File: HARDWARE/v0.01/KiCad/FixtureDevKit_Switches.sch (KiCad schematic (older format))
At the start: 64 parts, among them J10 LED_3, J106 LED_6, J107 LED_7, J11 SW_5, J12 LED_4, J13 SW_6, J14 LED_5, J15 SW_7, J2 LED_0, J3 SW_0, J4 SW_1, J5 LED_1, J6 SW_2, J7 LED_2, J8 SW_3, J9 SW_4, SW1 GTS203211B, SW2 GTS203211B, SW3 GTS203211B, SW4 GTS203211B, SW5 GTS203211B, SW6 GTS203211B, SW7 GTS203211B, SW8 GTS203211B

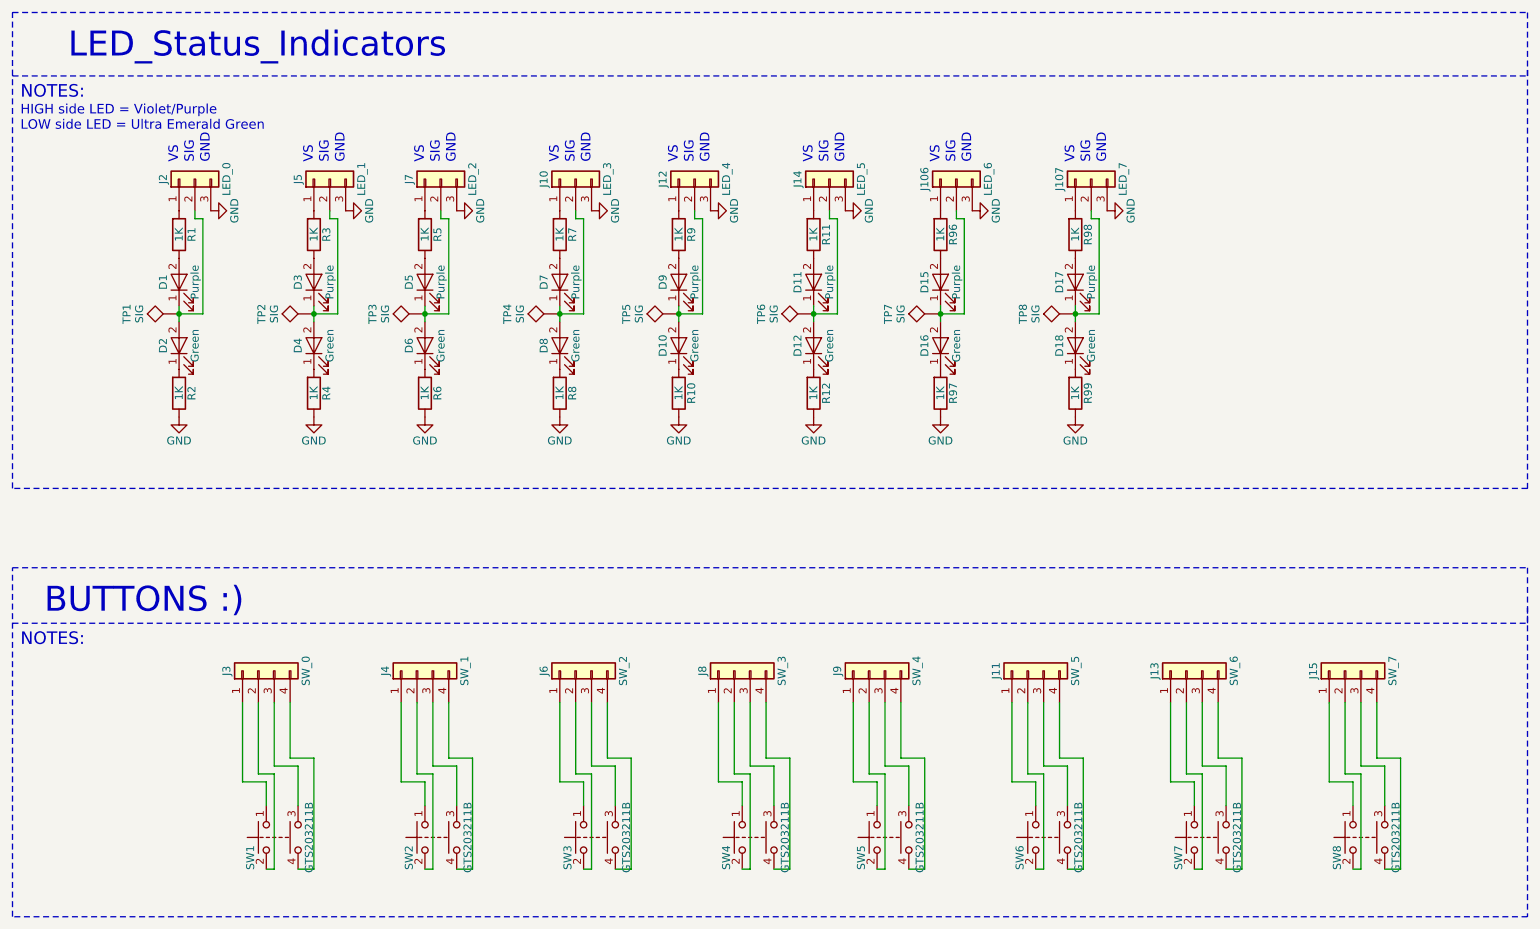
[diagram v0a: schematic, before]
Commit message: quasi-redoing entire schematic and layout
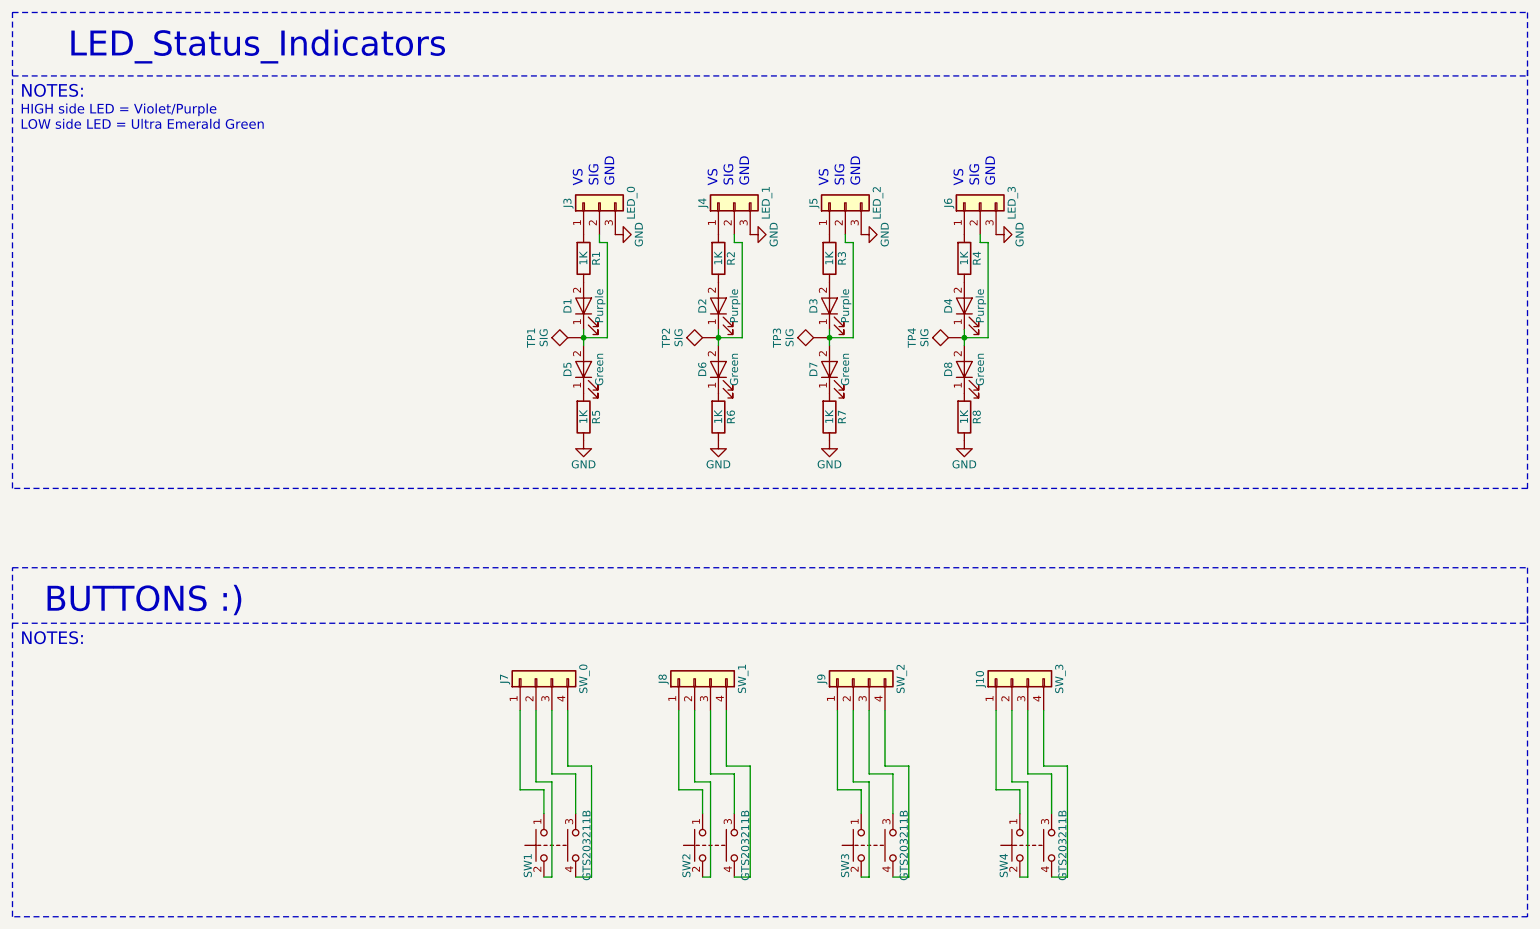
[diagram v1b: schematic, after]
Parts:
- removed D10, D12, D16, D18: Green, LEDs:LED_0805_HandSoldering, symbol LED
- removed D11, D15, D17, D9: Purple, LEDs:LED_0805_HandSoldering, symbol LED
- removed J106: LED_6, Pin_Headers:Pin_Header_Straight_1x03_Pitch2.54mm, symbol Conn_01x03
- removed J107: LED_7, Pin_Headers:Pin_Header_Straight_1x03_Pitch2.54mm, symbol Conn_01x03
- removed J11: SW_5, Pin_Headers:Pin_Header_Straight_1x04_Pitch2.54mm, symbol Conn_01x04
- removed J12: LED_4, Pin_Headers:Pin_Header_Straight_1x03_Pitch2.54mm, symbol Conn_01x03
- removed J13: SW_6, Pin_Headers:Pin_Header_Straight_1x04_Pitch2.54mm, symbol Conn_01x04
- removed J14: LED_5, Pin_Headers:Pin_Header_Straight_1x03_Pitch2.54mm, symbol Conn_01x03
- removed J15: SW_7, Pin_Headers:Pin_Header_Straight_1x04_Pitch2.54mm, symbol Conn_01x04
- removed J9: SW_4, Pin_Headers:Pin_Header_Straight_1x04_Pitch2.54mm, symbol Conn_01x04
- removed R10, R11, R12, R9, R96, R97, R98, R99: 1K, Resistors_SMD:R_0805_HandSoldering, symbol R
- removed SW5, SW6, SW7, SW8: GTS203211B, symbol SW_Push_Dual
- removed TP5, TP6, TP7, TP8: SIG, TestPoint:TestPoint, symbol TEST
- renumbered D3 to D2, D5 to D3, D7 to D4, D2 to D5, D4 to D6, D6 to D7, J8 to J10, J2 to J3, J5 to J4, J7 to J5, J10 to J6, J3 to J7, J4 to J8, J6 to J9, R3 to R2, R5 to R3, R7 to R4, R2 to R5, R4 to R6, R6 to R7
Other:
- moved on the sheet: D1, D2, D3, D4, D5, D6, D7, D8, J10, J3, J4, J5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

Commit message: updating layout footprints and board outline
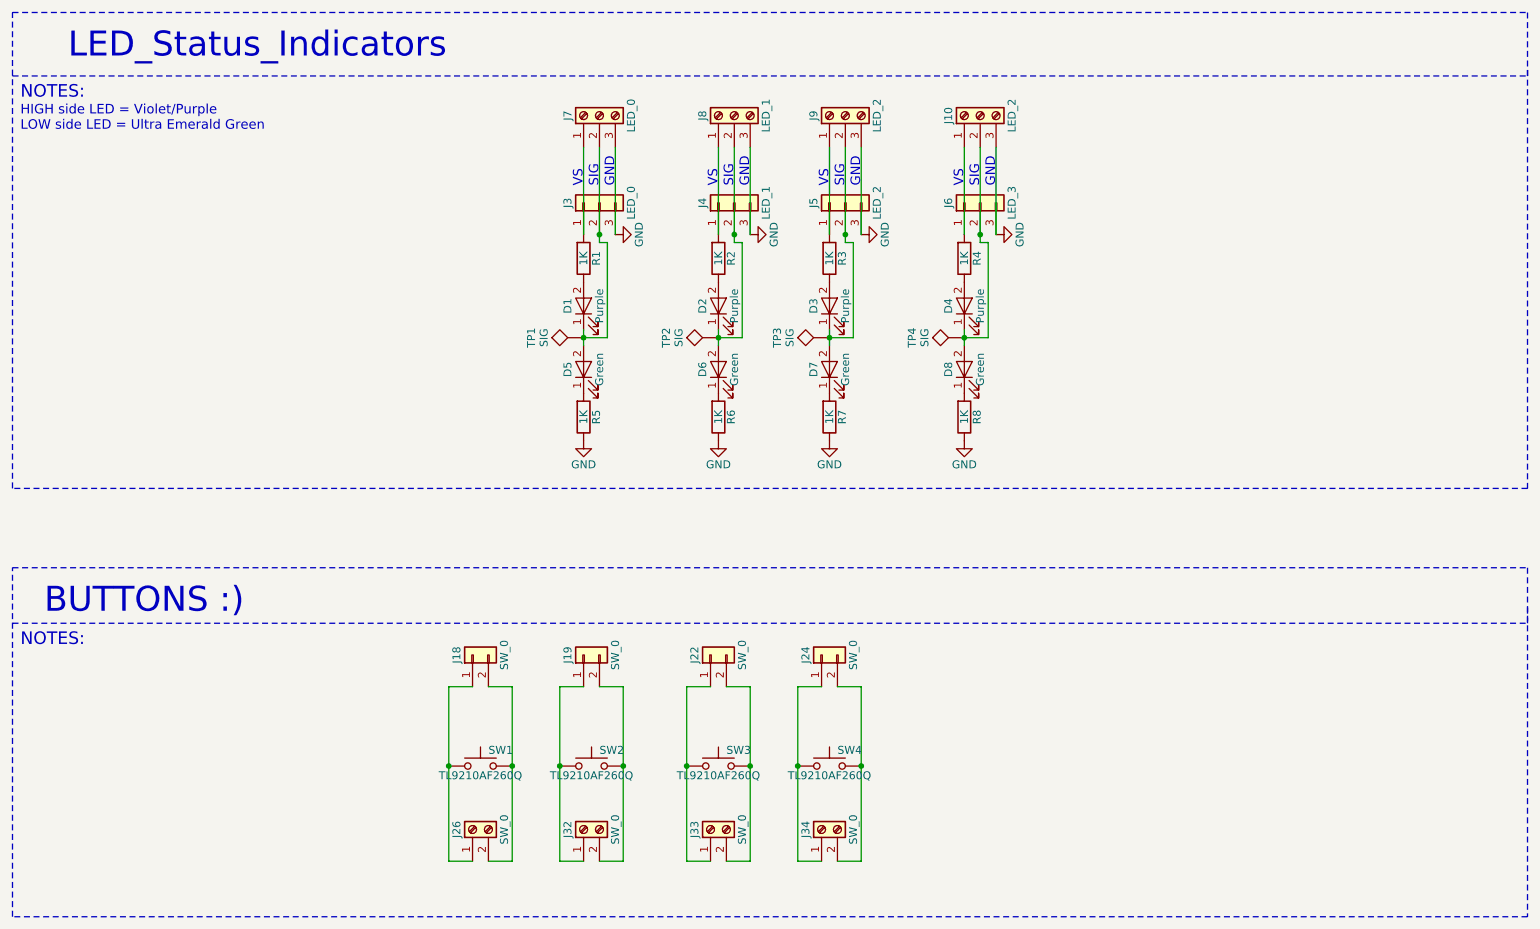
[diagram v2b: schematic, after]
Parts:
- removed J10: SW_3, Pin_Headers:Pin_Header_Straight_1x04_Pitch2.54mm, symbol Conn_01x04
- removed J7: SW_0, Pin_Headers:Pin_Header_Straight_1x04_Pitch2.54mm, symbol Conn_01x04
- removed J8: SW_1, Pin_Headers:Pin_Header_Straight_1x04_Pitch2.54mm, symbol Conn_01x04
- removed J9: SW_2, Pin_Headers:Pin_Header_Straight_1x04_Pitch2.54mm, symbol Conn_01x04
- removed SW1, SW2, SW3, SW4: GTS203211B, symbol SW_Push_Dual
- added J10, J9: LED_2, TerminalBlocks_Phoenix:TerminalBlock_Phoenix_MPT-2.54mm_3pol, symbol Screw_Terminal_01x03
- added J18, J19, J22, J24: SW_0, Pin_Headers:Pin_Header_Straight_2x01_Pitch2.54mm, symbol Conn_01x02
- added J26, J32, J33, J34: SW_0, TerminalBlocks:2Pin5.08, symbol Screw_Terminal_01x02
- added J7: LED_0, TerminalBlocks_Phoenix:TerminalBlock_Phoenix_MPT-2.54mm_3pol, symbol Screw_Terminal_01x03
- added J8: LED_1, TerminalBlocks_Phoenix:TerminalBlock_Phoenix_MPT-2.54mm_3pol, symbol Screw_Terminal_01x03
- added SW1, SW2, SW3, SW4: TL9210AF260Q, TL9210AF260Q:TL9210AF260Q, symbol SW_Push
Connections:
- net GND: now also J10.3 (Pin_3), J7.3 (Pin_3), J8.3 (Pin_3), J9.3 (Pin_3)
- net at J3.1 (Pin_1), R1.2: now also J7.1 (Pin_1)
- net at D1.1 (K), D5.2 (A), J3.2 (Pin_2)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: now also J7.2 (Pin_2)
- net at J4.1 (Pin_1), R2.2: now also J8.1 (Pin_1)
- net at D2.1 (K), D6.2 (A), J4.2 (Pin_2)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: now also J8.2 (Pin_2)
- net at J5.1 (Pin_1), R3.2: now also J9.1 (Pin_1)
- net at D3.1 (K), D7.2 (A), J5.2 (Pin_2)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: now also J9.2 (Pin_2)
- net at J6.1 (Pin_1), R4.2: now also J10.1 (Pin_1)
- net at D4.1 (K), D8.2 (A), J6.2 (Pin_2)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: now also J10.2 (Pin_2)
- new net: J18.1 (Pin_1), J26.1 (Pin_1), SW1.1
- new net: J18.2 (Pin_2), J26.2 (Pin_2), SW1.2
- new net: J19.1 (Pin_1), J32.1 (Pin_1), SW2.1
- new net: J19.2 (Pin_2), J32.2 (Pin_2), SW2.2
- new net: J22.1 (Pin_1), J33.1 (Pin_1), SW3.1
- new net: J22.2 (Pin_2), J33.2 (Pin_2), SW3.2
- new net: J24.1 (Pin_1), J34.1 (Pin_1), SW4.1
- new net: J24.2 (Pin_2), J34.2 (Pin_2), SW4.2

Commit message: updaing LED screw terminal foot print
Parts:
- J10: value LED_2 -> LED_3; footprint TerminalBlocks_Phoenix:TerminalBlock_Phoenix_MPT-2.54mm_3pol -> TerminalBlocks:3Pin5.08
- J7, J8, J9: footprint TerminalBlocks_Phoenix:TerminalBlock_Phoenix_MPT-2.54mm_3pol -> TerminalBlocks:3Pin5.08
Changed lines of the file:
@@
 F 0 "J7" H 4400 1400 50  0000 C CNN
 F 1 "LED_0" H 4400 1000 50  0000 C CNN
-F 2 "TerminalBlocks_Phoenix:TerminalBlock_Phoenix_MPT-2.54mm_3pol" H 4400 1200 50  0001 C CNN
+F 2 "TerminalBlocks:3Pin5.08" H 4400 1200 50  0001 C CNN
 F 3 "" H 4400 1200 50  0001 C CNN
 	1    4400 1200
@@
 F 0 "J8" H 5250 1400 50  0000 C CNN
 F 1 "LED_1" H 5250 1000 50  0000 C CNN
-F 2 "TerminalBlocks_Phoenix:TerminalBlock_Phoenix_MPT-2.54mm_3pol" H 5250 1200 50  0001 C CNN
+F 2 "TerminalBlocks:3Pin5.08" H 5250 1200 50  0001 C CNN
 F 3 "" H 5250 1200 50  0001 C CNN
 	1    5250 1200
@@
 F 0 "J9" H 5950 1400 50  0000 C CNN
 F 1 "LED_2" H 5950 1000 50  0000 C CNN
-F 2 "TerminalBlocks_Phoenix:TerminalBlock_Phoenix_MPT-2.54mm_3pol" H 5950 1200 50  0001 C CNN
+F 2 "TerminalBlocks:3Pin5.08" H 5950 1200 50  0001 C CNN
 F 3 "" H 5950 1200 50  0001 C CNN
 	1    5950 1200
@@
 P 6800 1200
 F 0 "J10" H 6800 1400 50  0000 C CNN
-F 1 "LED_2" H 6800 1000 50  0000 C CNN
-F 2 "TerminalBlocks_Phoenix:TerminalBlock_Phoenix_MPT-2.54mm_3pol" H 6800 1200 50  0001 C CNN
+F 1 "LED_3" H 6800 1000 50  0000 C CNN
+F 2 "TerminalBlocks:3Pin5.08" H 6800 1200 50  0001 C CNN
 F 3 "" H 6800 1200 50  0001 C CNN
 	1    6800 1200
